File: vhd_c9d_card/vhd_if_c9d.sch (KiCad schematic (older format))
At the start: 76 parts, among them IC1 80C49C, IC10 74LS04, IC11 SN751701P, IC12 74H004P, IC2 8255A, IC3 27C256, IC5 74LS30, IC6 74LS30, IC7 74LS27, IC8 74LS32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

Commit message: Add files via upload
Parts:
- removed L3: L, Inductor_THT:L_Axial_L5.0mm_D3.6mm_P10.00mm_Horizontal_Murata_BL01RN1A2A2, symbol agg-kicad:L
- added FL6, FL7, FL8, FL9: EMI_Filter_LCL, Connector_PinHeader_2.54mm:PinHeader_1x03_P2.54mm_Vertical, symbol Device:EMI_Filter_LCL
- J1: symbol connector2:DIN41612_03x32_ABC -> vhd_if_c9d-rescue:DIN41612_03x32_ABC-connector2
- Q1, Q2: symbol agg-kicad:NPN -> Device:Q_NPN_BCE
- Q3: symbol agg-kicad:PNP -> Device:Q_PNP_BEC
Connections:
- net A26: now also Q3.3 (C); no longer Q3.2 (E)
- net B8: now also Q1.2 (C); no longer Q1.3 (C)
- net GND: now also L1.2, Q1.3 (E), Q2.3 (E), Q3.2 (E), FL6.2, FL7.2, FL8.2, FL9.2; no longer J2.1, J2.7, Q1.2 (E), Q2.2 (E), Q3.3 (C)
- net S2: now also FL8.1; no longer J2.2
- net S3: now also FL9.1; no longer J2.3
- net VHD6: now also FL6.1
- net VHD7: now also FL7.1; no longer L1.2
- net at D3.2, D4.1, FL2.3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: now also Q2.2 (C); no longer Q2.3 (C)
- net at J3.7: now also FL7.3; no longer L1.1
- net at J3.6: now also FL6.3
- new net: J2.1, J2.7, L1.1
- new net: FL8.3, J2.2
- new net: FL9.3, J2.3
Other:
- moved on the sheet: J2, R13

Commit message: Add files via upload
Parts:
- J3: footprint Connector_Dsub:DSUB-15_Female_Horizontal_P2.77x2.84mm_EdgePinOffset4.94mm_Housed_MountingHolesOffset7.48mm -> Connector_Dsub:DSUB-15_Female_Horizontal_P2.77x2.84mm_EdgePinOffset7.70mm_Housed_MountingHolesOffset9.12mm
- R19: value 750K -> 1M
- R4: value 10K -> 27K
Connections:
- net RESET_ is gone; now on net A6: IC1.4 (~RESET~), IC12.9, R16.2
- no-connect marks 38 -> 36
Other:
- note added: "3= notch side"
- note added: "3=notch side"
- note added: "C5"
- note added: "C6"
- note added: "R02"
- note added: "R03"
- note added: "R05"
- note added: "R06"
- note added: "R07"
- note added: "R08"
- note added: "R09"
- note added: "R1"
- note added: "R10"
- note added: "R13"
- note added: "R14"
- note added: "R15"
- note added: "R27"
- note added: "R28"
- note added: "R29"
- note added: "R30"
- note added: "R32"
- note added: "R33"
- note added: "RESET"
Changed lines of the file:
@@
 U 3 1 629B3029
 P 7000 10500
-F 0 "IC12" H 7000 10817 50  0000 C CNN
-F 1 "74H004P" H 7000 10726 50  0000 C CNN
+F 0 "IC12" H 6950 10800 50  0000 C CNN
+F 1 "74H004P" H 6900 10700 50  0000 C CNN
 F 2 "" H 7000 10500 50  0001 C CNN
 F 3 "https://assets.nexperia.com/documents/data-sheet/74HC_HCT04.pdf" H 7000 10500 50  0001 C CNN
@@
 P 7000 10250
 F 0 "R19" H 7050 10300 50  0000 C CNN
-F 1 "750K" H 7050 10200 50  0000 C CNN
+F 1 "1M" H 7050 10200 50  0000 C CNN
 F 2 "Resistor_THT:R_Axial_DIN0204_L3.6mm_D1.6mm_P7.62mm_Horizontal" H 7000 10250 50  0001 C CNN
 F 3 "" H 7000 10250 50  0001 C CNN
@@
 F 0 "J3" H 5104 1446 50  0000 L CNN
 F 1 "DB15_Female" H 5104 1355 50  0000 L CNN
-F 2 "Connector_Dsub:DSUB-15_Female_Horizontal_P2.77x2.84mm_EdgePinOffset4.94mm_Housed_MountingHolesOffset7.48mm" H 4950 1400 50  0001 C CNN
+F 2 "Connector_Dsub:DSUB-15_Female_Horizontal_P2.77x2.84mm_EdgePinOffset7.70mm_Housed_MountingHolesOffset9.12mm" H 4950 1400 50  0001 C CNN
 F 3 " ~" H 4950 1400 50  0001 C CNN
 	1    4950 1400
@@
 P 1950 1100
 F 0 "R4" H 2000 1150 50  0000 C CNN
-F 1 "10K" H 2000 1050 50  0000 C CNN
+F 1 "27K" H 2000 1050 50  0000 C CNN
 F 2 "Resistor_THT:R_Axial_DIN0204_L3.6mm_D1.6mm_P7.62mm_Horizontal" H 1950 1100 50  0001 C CNN
 F 3 "" H 1950 1100 50  0001 C CNN
@@
 	5400 8000 5400 7950
 NoConn ~ 8800 6300
-NoConn ~ 6200 8700
-NoConn ~ 6200 8650
 $Comp
 L 4xxx:4013 #IC17
@@
 $EndComp
 Wire Wire Line
-	10350 50   10350 -50
-Wire Wire Line
 	10300 1800 10300 1700
 Wire Wire Line
-	10000 50   10350 50
-Connection ~ 10350 50
-Wire Wire Line
-	10350 50   10700 50
-Wire Wire Line
-	10000 -250 10700 -250
-Wire Wire Line
 	10300 2000 10300 1900
 Connection ~ 11750 1700
@@
 Wire Wire Line
 	2950 500  3350 500
+Text Notes 10000 2150 0    50   ~ 0
+3= notch side
+Text Notes 9050 7850 0    50   ~ 0
+3=notch side
+Text Notes 2900 2750 0    50   ~ 0
+R10
+Text Notes 4350 3700 0    50   ~ 0
+R1
+Text Notes 2050 1050 0    50   ~ 0
+R33
+Text Notes 2950 8400 0    50   ~ 0
+R13
+Text Notes 6050 5650 0    50   ~ 0
+R09
+Text Notes 9450 2000 0    50   ~ 0
+R32
+Text Notes 9400 2400 0    50   ~ 0
+R02
+Text Notes 9250 7400 0    50   ~ 0
+R03
+Text Notes 9750 6900 0    50   ~ 0
+R06
+Text Notes 9400 6550 0    50   ~ 0
+R05
+Text Notes 3850 10300 0    50   ~ 0
+R08
+Text Notes 6000 10150 0    50   ~ 0
+R07
+Text Notes 7150 10200 0    50   ~ 0
+R15
+Text Notes 6200 11000 0    50   ~ 0
+R14
+Text Notes 2650 9500 0    50   ~ 0
+R28
+Text Notes 1600 9500 0    50   ~ 0
+R30
+Text Notes 2000 10400 0    50   ~ 0
+R29
+Text Notes 2700 10950 0    50   ~ 0
+R27
+Text Notes 7600 10750 0    50   ~ 0
+C6
+Text Notes 6500 10600 0    50   ~ 0
+C5
+Text GLabel 4400 6800 0    50   Input ~ 0
+A6
+Text Notes 4350 6950 2    50   ~ 0
+RESET
 $EndSCHEMATC

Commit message: Add files via upload
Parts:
- IC2: value 8255A -> NEC D8255AC-2
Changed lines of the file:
@@
 P 8100 5600
 F 0 "IC2" H 8100 7381 50  0000 C CNN
-F 1 "8255A" H 8100 7290 50  0000 C CNN
+F 1 "NEC D8255AC-2" H 8000 7250 50  0000 C CNN
 F 2 "Package_DIP:DIP-40_W15.24mm_Socket" H 8100 5900 50  0001 C CNN
 F 3 "http://aturing.umcs.maine.edu/~meadow/courses/cos335/Intel8255A.pdf" H 8100 5900 50  0001 C CNN

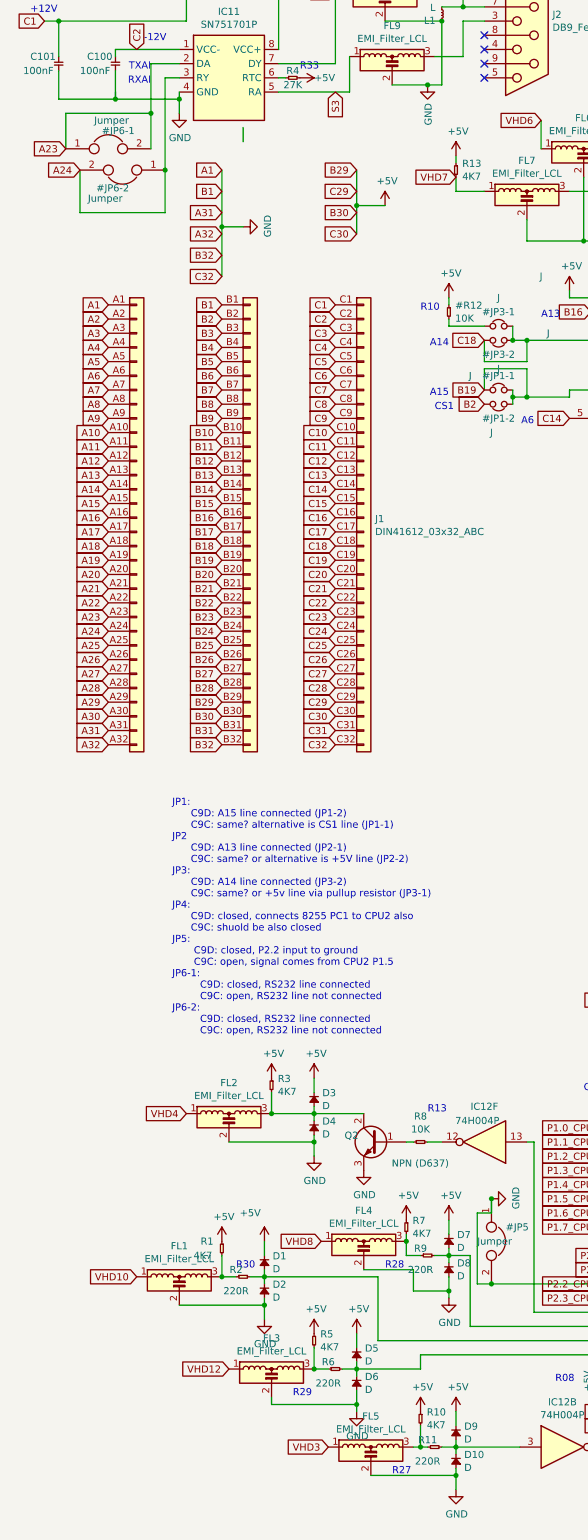
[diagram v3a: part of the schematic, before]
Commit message: Add files via upload
now reset line is also connected in pcb and some component movement done near crystal.
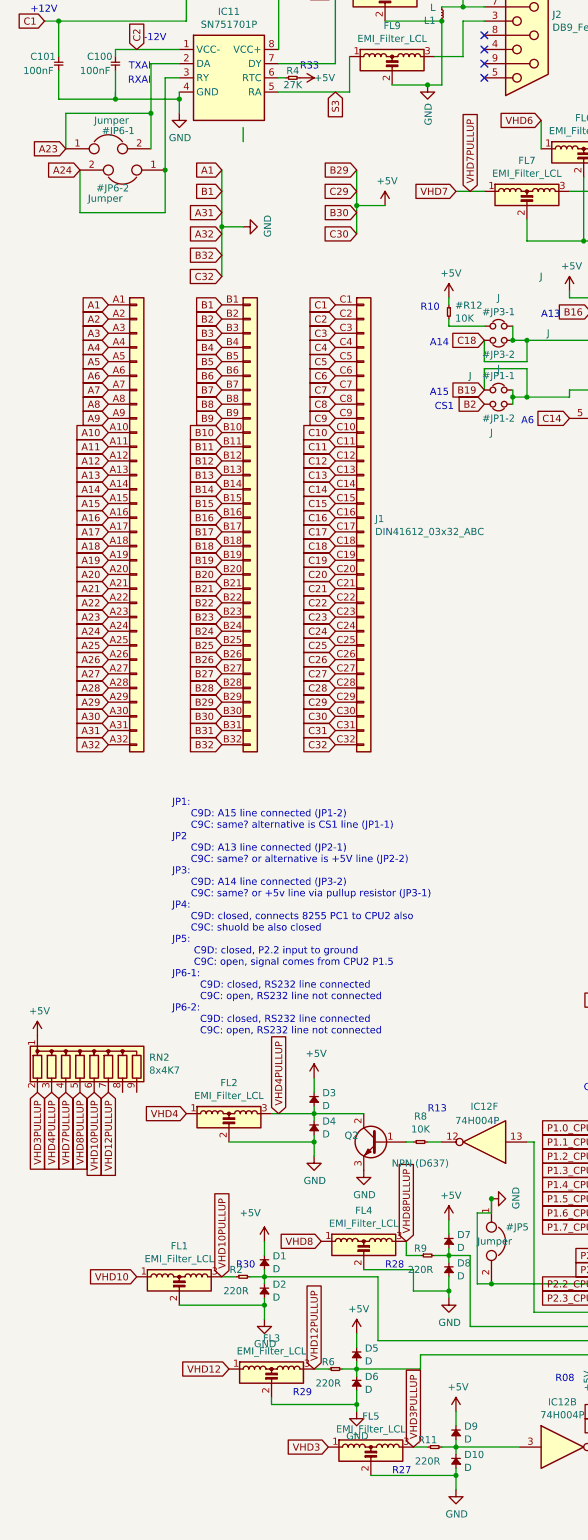
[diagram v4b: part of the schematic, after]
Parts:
- removed R1, R10, R13, R3, R5, R7: 4K7, Resistor_THT:R_Axial_DIN0204_L3.6mm_D1.6mm_P7.62mm_Horizontal, symbol agg-kicad:R
- added RN2: 8x4K7, Resistor_THT:R_Array_SIP9, symbol Device:R_Network08
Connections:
- net +5V: now also RN2.1 (common)
- net VHD7: now also RN2.4 (R3)
- net VHD4PULLUP: now reaches D3.2, D4.1, FL2.3, Q2.2 (C)
- net VHD4PULLUP: now also RN2.3 (R2)
- net VHD3PULLUP: now reaches FL5.3, R11.1
- net VHD3PULLUP: now also RN2.2 (R1)
- net VHD12PULLUP: now reaches FL3.3, R6.1
- net VHD12PULLUP: now also RN2.7 (R6)
- net VHD10PULLUP: now reaches FL1.3, R2.1
- net VHD10PULLUP: now also RN2.6 (R5)
- net VHD8PULLUP: now reaches FL4.3, R9.1
- net VHD8PULLUP: now also RN2.5 (R4)
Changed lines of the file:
@@
 encoding utf-8
 Sheet 1 1
-Title "Victor VHD IF-C9D"
+Title "Victor VHD IF-C9D by Popolon_"
 Date ""
 Rev ""
 Comp ""
-Comment1 ""
+Comment1 "Copied from original PCB"
 Comment2 ""
 Comment3 ""
@@
 	2800 8600 2850 8600
 $Comp
-L agg-kicad:R R3
-U 1 1 634102E4
-P 1850 8150
-F 0 "R3" V 1854 8194 50  0000 L CNN
-F 1 "4K7" V 1945 8194 50  0000 L CNN
-F 2 "Resistor_THT:R_Axial_DIN0204_L3.6mm_D1.6mm_P7.62mm_Horizontal" H 1850 8150 50  0001 C CNN
-F 3 "" H 1850 8150 50  0001 C CNN
-	1    1850 8150
-	0    1    1    0
-$EndComp
-$Comp
-L power:+5V #PWR06
-U 1 1 6341108C
-P 1850 8150
-F 0 "#PWR06" H 1850 8000 50  0001 C CNN
-F 1 "+5V" H 1865 8323 50  0000 C CNN
-F 2 "" H 1850 8150 50  0001 C CNN
-F 3 "" H 1850 8150 50  0001 C CNN
-	1    1850 8150
-	1    0    0    -1
-$EndComp
-$Comp
 L agg-kicad:D D4
 U 1 1 6341A4BB
@@
 Wire Wire Line
 	2150 8400 1850 8400
-Wire Wire Line
-	1850 8250 1850 8400
 Text GLabel 1250 8400 0    50   Input ~ 0
 VHD4
@@
 	5850 10500 5900 10500
 $Comp
-L agg-kicad:R R1
-U 1 1 634E62E5
-P 1500 9300
-F 0 "R1" V 1500 9150 50  0000 L CNN
-F 1 "4K7" V 1600 9100 50  0000 L CNN
-F 2 "Resistor_THT:R_Axial_DIN0204_L3.6mm_D1.6mm_P7.62mm_Horizontal" H 1500 9300 50  0001 C CNN
-F 3 "" H 1500 9300 50  0001 C CNN
-	1    1500 9300
-	0    1    1    0
-$EndComp
-$Comp
-L power:+5V #PWR03
-U 1 1 634E62EB
-P 1500 9300
-F 0 "#PWR03" H 1500 9150 50  0001 C CNN
-F 1 "+5V" H 1515 9473 50  0000 C CNN
-F 2 "" H 1500 9300 50  0001 C CNN
-F 3 "" H 1500 9300 50  0001 C CNN
-	1    1500 9300
-	1    0    0    -1
-$EndComp
-$Comp
 L agg-kicad:D D2
 U 1 1 634E62F1
@@
 Wire Wire Line
 	1800 9550 1700 9550
-Wire Wire Line
-	1500 9400 1500 9550
 Text GLabel 900  9550 0    50   Input ~ 0
 VHD10
@@
 	1600 9550 1500 9550
 $Comp
-L agg-kicad:R R5
-U 1 1 635154C6
-P 2150 9950
-F 0 "R5" V 2154 9994 50  0000 L CNN
-F 1 "4K7" V 2245 9994 50  0000 L CNN
-F 2 "Resistor_THT:R_Axial_DIN0204_L3.6mm_D1.6mm_P7.62mm_Horizontal" H 2150 9950 50  0001 C CNN
-F 3 "" H 2150 9950 50  0001 C CNN
-	1    2150 9950
-	0    1    1    0
-$EndComp
-$Comp
-L power:+5V #PWR011
-U 1 1 635154CC
-P 2150 9950
-F 0 "#PWR011" H 2150 9800 50  0001 C CNN
-F 1 "+5V" H 2165 10123 50  0000 C CNN
-F 2 "" H 2150 9950 50  0001 C CNN
-F 3 "" H 2150 9950 50  0001 C CNN
-	1    2150 9950
-	1    0    0    -1
-$EndComp
-$Comp
 L agg-kicad:D D6
 U 1 1 635154D2
@@
 	2450 10200 2450 10250
 Wire Wire Line
-	2150 10050 2150 10200
-Wire Wire Line
 	2900 10200 2450 10200
 Text GLabel 1550 10200 0    50   Input ~ 0
 VHD12
 $Comp
-L agg-kicad:R R7
-U 1 1 63552C50
-P 2800 9150
-F 0 "R7" V 2804 9194 50  0000 L CNN
-F 1 "4K7" V 2895 9194 50  0000 L CNN
-F 2 "Resistor_THT:R_Axial_DIN0204_L3.6mm_D1.6mm_P7.62mm_Horizontal" H 2800 9150 50  0001 C CNN
-F 3 "" H 2800 9150 50  0001 C CNN
-	1    2800 9150
-	0    1    1    0
-$EndComp
-$Comp
-L power:+5V #PWR016
-U 1 1 63552C56
-P 2800 9150
-F 0 "#PWR016" H 2800 9000 50  0001 C CNN
-F 1 "+5V" H 2815 9323 50  0000 C CNN
-F 2 "" H 2800 9150 50  0001 C CNN
-F 3 "" H 2800 9150 50  0001 C CNN
-	1    2800 9150
-	1    0    0    -1
-$EndComp
-$Comp
 L agg-kicad:D D8
 U 1 1 63552C5C
@@
 Wire Wire Line
 	3100 9400 3100 9450
-Wire Wire Line
-	2800 9250 2800 9300
 Text GLabel 2200 9300 0    50   Input ~ 0
 VHD8
@@
 	2900 10100 2900 10200
 $Comp
-L agg-kicad:R R13
-U 1 1 6358448A
-P 3150 1700
-F 0 "R13" V 3154 1744 50  0000 L CNN
-F 1 "4K7" V 3245 1744 50  0000 L CNN
-F 2 "Resistor_THT:R_Axial_DIN0204_L3.6mm_D1.6mm_P7.62mm_Horizontal" H 3150 1700 50  0001 C CNN
-F 3 "" H 3150 1700 50  0001 C CNN
-	1    3150 1700
-	0    1    1    0
-$EndComp
-$Comp
-L power:+5V #PWR024
-U 1 1 6358C713
-P 3150 1650
-F 0 "#PWR024" H 3150 1500 50  0001 C CNN
-F 1 "+5V" H 3165 1823 50  0000 C CNN
-F 2 "" H 3150 1650 50  0001 C CNN
-F 3 "" H 3150 1650 50  0001 C CNN
-	1    3150 1650
-	1    0    0    -1
-$EndComp
-Wire Wire Line
-	3150 1700 3150 1650
-$Comp
 L power:GND #PWR02
 U 1 1 635C9CAA
@@
 	1    0    0    -1
 $EndComp
-Wire Wire Line
-	2850 10750 2900 10750
-$Comp
-L agg-kicad:R R10
-U 1 1 63DB3DE0
-P 2900 10500
-F 0 "R10" V 2904 10544 50  0000 L CNN
-F 1 "4K7" V 2995 10544 50  0000 L CNN
-F 2 "Resistor_THT:R_Axial_DIN0204_L3.6mm_D1.6mm_P7.62mm_Horizontal" H 2900 10500 50  0001 C CNN
-F 3 "" H 2900 10500 50  0001 C CNN
-	1    2900 10500
-	0    1    1    0
-$EndComp
-$Comp
-L power:+5V #PWR017
-U 1 1 63DB3DE6
-P 2900 10500
-F 0 "#PWR017" H 2900 10350 50  0001 C CNN
-F 1 "+5V" H 2915 10673 50  0000 C CNN
-F 2 "" H 2900 10500 50  0001 C CNN
-F 3 "" H 2900 10500 50  0001 C CNN
-	1    2900 10500
-	1    0    0    -1
-$EndComp
-Wire Wire Line
-	2900 10600 2900 10750
 $Comp
 L power:GND #PWR037
@@
 Wire Wire Line
 	11850 7500 11750 7500
-Text GLabel 3150 1800 0    50   Input ~ 0
+Text GLabel 3150 1900 0    50   Input ~ 0
 VHD7
 $Comp
@@
 	1    0    0    -1
 $EndComp
-Connection ~ 2150 10200
 Wire Wire Line
 	2450 10450 1850 10450
@@
 	1    0    0    -1
 $EndComp
-Connection ~ 1500 9550
 Wire Wire Line
 	1200 9750 1800 9750
@@
 	1    0    0    -1
 $EndComp
-Connection ~ 2800 9300
 Wire Wire Line
 	2800 9300 2800 9400
@@
 	1    0    0    -1
 $EndComp
-Connection ~ 1850 8400
 Wire Wire Line
 	1550 8600 2150 8600
@@
 	1    0    0    -1
 $EndComp
-Connection ~ 2900 10750
-Wire Wire Line
-	2900 10750 2950 10750
 Text GLabel 250  700  0    50   Input ~ 0
 C1
@@
 Wire Wire Line
 	3350 1900 3150 1900
-Wire Wire Line
-	3150 1800 3150 1900
 $Comp
 L Device:EMI_Filter_LCL FL7
@@
 Text Notes 4350 6950 2    50   ~ 0
 RESET
+$Comp
+L Device:R_Network08 RN2
+U 1 1 63A5B821
+P 600 8050
+F 0 "RN2" H 988 8096 50  0000 L CNN
+F 1 "8x4K7" H 988 8005 50  0000 L CNN
+F 2 "Resistor_THT:R_Array_SIP9" V 1075 8050 50  0001 C CNN
+F 3 "http://www.vishay.com/docs/31509/csc.pdf" H 600 8050 50  0001 C CNN
+	1    600  8050
+	1    0    0    -1
+$EndComp
+$Comp
+L power:+5V #PWR?
+U 1 1 63A5B82F
+P 200 7850
+F 0 "#PWR?" H 200 7700 50  0001 C CNN
+F 1 "+5V" H 215 8023 50  0000 C CNN
+F 2 "" H 200 7850 50  0001 C CNN
+F 3 "" H 200 7850 50  0001 C CNN
+	1    200  7850
+	1    0    0    -1
+$EndComp
+Text GLabel 200  8250 3    50   Input ~ 0
+VHD3PULLUP
+Text GLabel 300  8250 3    50   Input ~ 0
+VHD4PULLUP
+Text GLabel 500  8250 3    50   Input ~ 0
+VHD8PULLUP
+Text GLabel 600  8250 3    50   Input ~ 0
+VHD10PULLUP
+Text GLabel 700  8250 3    50   Input ~ 0
+VHD12PULLUP
+Text GLabel 400  8250 3    50   Input ~ 0
+VHD7PULLUP
+Text GLabel 2850 10750 1    50   Input ~ 0
+VHD3PULLUP
+Wire Wire Line
+	2850 10750 2950 10750
+Text GLabel 2150 10200 1    50   Input ~ 0
+VHD12PULLUP
+Text GLabel 2800 9300 1    50   Input ~ 0
+VHD8PULLUP
+Text GLabel 1900 8400 1    50   Input ~ 0
+VHD4PULLUP
+Text GLabel 1500 9550 1    50   Input ~ 0
+VHD10PULLUP
+Text GLabel 3250 1900 1    50   Input ~ 0
+VHD7PULLUP
 $EndSCHEMATC

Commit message: Add files via upload
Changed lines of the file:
@@
 $EndComp
 $Comp
-L 4xxx:4538 #IC12
+L 4xxx:4538 #IC18
 U 2 1 63ACCA7B
 P 13900 3050
-F 0 "#IC12" H 13900 3517 50  0000 C CNN
+F 0 "#IC18" H 13900 3517 50  0000 C CNN
 F 1 "4538" H 13900 3426 50  0000 C CNN
 F 2 "Package_DIP:DIP-16_W7.62mm_Socket" H 13900 3050 50  0001 C CNN
